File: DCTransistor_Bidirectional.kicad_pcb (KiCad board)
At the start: 2 copper layers, 457.2 x 457.2 mm, 282 parts, among them J0 USB_C_Receptacle, Q0 MMBT3904, Q1 MMBT3904, Q2 AOD403, U0 CH340C, U2 ESP-12F, U3 SN74LVC1T45DBV, U4 TLV70233DBVR

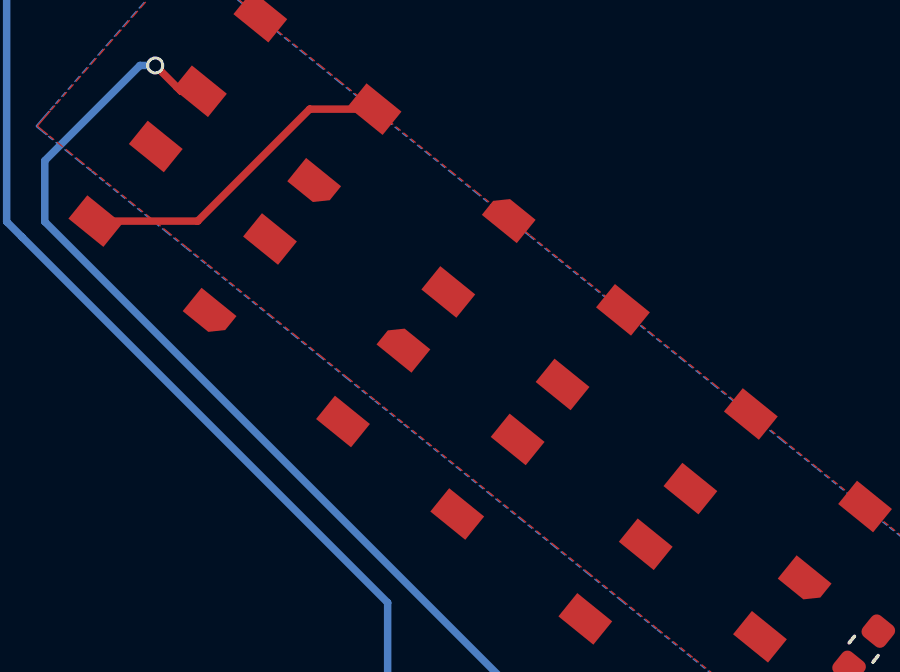
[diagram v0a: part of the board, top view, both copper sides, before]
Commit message: layout fixes and schematic re-sync with layout
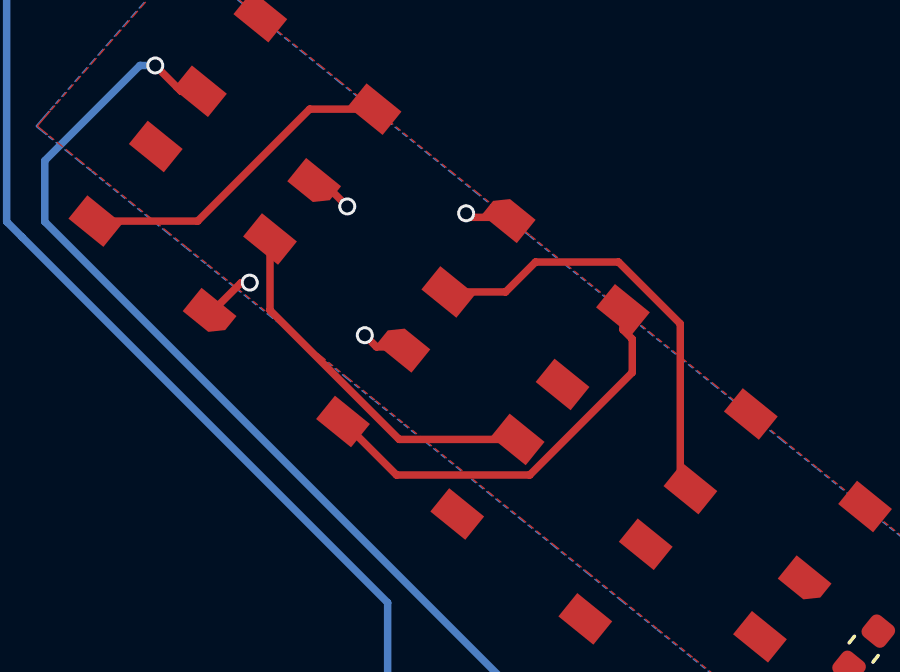
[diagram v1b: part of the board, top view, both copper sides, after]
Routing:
- net (no net): track 0.00 -> 14.6 mm
- net Net-(D172-DOUT): track 0.00 -> 14.0 mm
- net Net-(D173-DOUT): track 0.00 -> 12.4 mm
- net GND: track 165.0 -> 171.1 mm, vias 3 -> 7

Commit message: layout updates
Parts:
- added TP2: 5016, jannett_footprints:TestPoint_Keystone_5016_Compact, F.Cu at (93.5, 371.7)
- added TP3: 5016, jannett_footprints:TestPoint_Keystone_5016_Compact, F.Cu at (94.8, 461.8)
- added TP4: 5016, jannett_footprints:TestPoint_Keystone_5016_Compact, F.Cu at (87.8, 461.8)
- added TP5: 5016, jannett_footprints:TestPoint_Keystone_5016_Compact, F.Cu at (101.8, 461.8)
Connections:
- D208 pad 4: unconnected-(D208-DOUT-Pad4) -> Net-(D208-DOUT)
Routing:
- net GND: track 171.1 -> 281.3 mm, vias 7 -> 79
- net +5V: track 279.4 -> 350.0 mm, vias 2 -> 5
- net Net-(D15-DOUT): track 0.00 -> 24.0 mm, vias 0 -> 2
- net Net-(D10-DIN): track 0.00 -> 21.1 mm, vias 0 -> 2
- net Net-(D17-DOUT): track 0.00 -> 19.9 mm, vias 0 -> 2
- net Net-(D11-DOUT): track 0.00 -> 17.1 mm, vias 0 -> 2
- net (no net): track 14.6 -> 0.00 mm
- net Net-(D172-DOUT): track 14.0 -> 0.00 mm
- net Net-(D13-DOUT): track 0.00 -> 14.0 mm, vias 0 -> 2
- net Net-(D14-DOUT): track 0.00 -> 13.4 mm, vias 0 -> 2
- net Net-(D173-DOUT): track 12.4 -> 0.00 mm
- net Net-(D8-DOUT): track 0.00 -> 10.9 mm, vias 0 -> 2
- net Net-(D10-DOUT): track 0.00 -> 10.9 mm, vias 0 -> 2
- net Net-(D12-DOUT): track 0.00 -> 10.9 mm, vias 0 -> 2
- net Net-(D174-DOUT): track 10.9 -> 0.00 mm
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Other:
- outline, holes or cut-outs redrawn
- board text added: "D2 DIN"
- board text added: "D208"
- board text added: "DOUT"

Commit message: layout updates
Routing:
- net Net-(D201-DOUT): track 0.00 -> 112.7 mm, vias 0 -> 2
- net Net-(D203-DOUT): track 0.00 -> 44.2 mm, vias 0 -> 2
- net Net-(D19-DOUT): track 0.00 -> 16.3 mm, vias 0 -> 2
- net Net-(D200-DOUT): track 0.00 -> 15.9 mm, vias 0 -> 2
- net Net-(D16-DOUT): track 0.00 -> 12.9 mm, vias 0 -> 2
- net GND: track 281.3 -> 293.6 mm, vias 79 -> 88
- net Net-(D18-DOUT): track 0.00 -> 11.1 mm, vias 0 -> 2
- net Net-(D202-DOUT): track 0.00 -> 11.0 mm, vias 0 -> 2
- net +5V: track 350.0 -> 352.1 mm
